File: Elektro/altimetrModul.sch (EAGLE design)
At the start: 16 parts, among them IC1 ATTINY1624-SSU, J1 SM04B-GHS-TB(LF)(SN)-

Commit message: Added Modules
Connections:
- net MISO: now also JP4.3
- net MOSI: no longer JP4.3
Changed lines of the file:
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@@
 <pinref part="JP2" gate="A" pin="6"/>
+</segment>
+<segment>
+<pinref part="JP4" gate="A" pin="3"/>
+<wire x1="-43.18" y1="48.26" x2="-50.8" y2="48.26" width="0.1524" layer="91"/>
+<label x="-50.8" y="48.26" size="1.27" layer="95" rot="R180" xref="yes"/>
 </segment>
 </net>
@@
 </segment>
 <segment>
-<wire x1="-43.18" y1="48.26" x2="-50.8" y2="48.26" width="0.1524" layer="91" grouprefs="FLASH"/>
-<label x="-50.8" y="48.26" size="1.27" layer="95" rot="R180" xref="yes" grouprefs="FLASH"/>
-<pinref part="JP4" gate="A" pin="3"/>
-</segment>
-<segment>

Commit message: Added names
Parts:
- renumbered JP2 to BMP_280, JP4 to FLASH_
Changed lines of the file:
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@@
 <part name="U$8" library="supply2" deviceset="+3.3V" device=""/>
 <part name="GND1" library="PUTRocketLab_supply" deviceset="GND" device=""/>
-<part name="JP2" library="pinhead" library_urn="urn:adsk.eagle:library:325" deviceset="PINHD-1X6" device="" package3d_urn="urn:adsk.eagle:package:22472/2"/>
-<part name="JP4" library="pinhead" library_urn="urn:adsk.eagle:library:325" deviceset="PINHD-1X6" device="" package3d_urn="urn:adsk.eagle:package:22472/2"/>
+<part name="BMP_280" library="pinhead" library_urn="urn:adsk.eagle:library:325" deviceset="PINHD-1X6" device="" package3d_urn="urn:adsk.eagle:package:22472/2"/>
+<part name="FLASH_" library="pinhead" library_urn="urn:adsk.eagle:library:325" deviceset="PINHD-1X6" device="" package3d_urn="urn:adsk.eagle:package:22472/2"/>
 <part name="U$5" library="supply2" deviceset="+3.3V" device=""/>
 <part name="U$7" library="supply2" deviceset="+3.3V" device=""/>
@@
 <attribute name="VALUE" x="-160.02" y="36.83" size="1.778" layer="96"/>
 </instance>
-<instance part="JP2" gate="A" x="60.96" y="96.52" smashed="yes" grouprefs="BMP280">
+<instance part="BMP_280" gate="A" x="60.96" y="96.52" smashed="yes" grouprefs="BMP280">
 <attribute name="NAME" x="54.61" y="107.315" size="1.778" layer="95"/>
 <attribute name="VALUE" x="54.61" y="86.36" size="1.778" layer="96"/>
 </instance>
-<instance part="JP4" gate="A" x="-40.64" y="45.72" smashed="yes" grouprefs="FLASH">
+<instance part="FLASH_" gate="A" x="-40.64" y="45.72" smashed="yes" grouprefs="FLASH">
 <attribute name="NAME" x="-46.99" y="56.515" size="1.778" layer="95"/>
 <attribute name="VALUE" x="-46.99" y="35.56" size="1.778" layer="96"/>
@@
 </segment>
 <segment>
-<pinref part="JP2" gate="A" pin="2"/>
+<pinref part="BMP_280" gate="A" pin="2"/>
 <pinref part="GND5" gate="1" pin="GND"/>
 <wire x1="38.1" y1="101.6" x2="58.42" y2="101.6" width="0.1524" layer="91" grouprefs="BMP280"/>
@@
 <pinref part="GND8" gate="1" pin="GND"/>
 <wire x1="-60.96" y1="43.18" x2="-60.96" y2="45.72" width="0.1524" layer="91" grouprefs="FLASH"/>
-<pinref part="JP4" gate="A" pin="4"/>
+<pinref part="FLASH_" gate="A" pin="4"/>
 <wire x1="-60.96" y1="45.72" x2="-43.18" y2="45.72" width="0.1524" layer="91" grouprefs="FLASH"/>
 </segment>
@@
 </segment>
 <segment>
-<pinref part="JP2" gate="A" pin="1"/>
+<pinref part="BMP_280" gate="A" pin="1"/>
 <wire x1="58.42" y1="104.14" x2="50.8" y2="104.14" width="0.1524" layer="91" grouprefs="BMP280"/>
 <pinref part="U$5" gate="G$1" pin="+3.3V"/>
 </segment>
 <segment>
-<pinref part="JP4" gate="A" pin="1"/>
+<pinref part="FLASH_" gate="A" pin="1"/>
 <wire x1="-43.18" y1="53.34" x2="-50.8" y2="53.34" width="0.1524" layer="91" grouprefs="FLASH"/>
 <pinref part="U$7" gate="G$1" pin="+3.3V"/>
@@
 <wire x1="58.42" y1="99.06" x2="50.8" y2="99.06" width="0.1524" layer="91" grouprefs="BMP280"/>
 <label x="50.8" y="99.06" size="1.27" layer="95" rot="R180" xref="yes" grouprefs="BMP280"/>
-<pinref part="JP2" gate="A" pin="3"/>
+<pinref part="BMP_280" gate="A" pin="3"/>
 </segment>
 <segment>
 <wire x1="-43.18" y1="43.18" x2="-50.8" y2="43.18" width="0.1524" layer="91" grouprefs="FLASH"/>
 <label x="-50.8" y="43.18" size="1.27" layer="95" rot="R180" xref="yes" grouprefs="FLASH"/>
-<pinref part="JP4" gate="A" pin="5"/>
+<pinref part="FLASH_" gate="A" pin="5"/>
 </segment>
 </net>
@@
 <wire x1="58.42" y1="91.44" x2="50.8" y2="91.44" width="0.1524" layer="91" grouprefs="BMP280"/>
 <label x="50.8" y="91.44" size="1.27" layer="95" rot="R180" xref="yes" grouprefs="BMP280"/>
-<pinref part="JP2" gate="A" pin="6"/>
-</segment>
-<segment>
-<pinref part="JP4" gate="A" pin="3"/>
+<pinref part="BMP_280" gate="A" pin="6"/>
+</segment>
+<segment>
+<pinref part="FLASH_" gate="A" pin="3"/>
 <wire x1="-43.18" y1="48.26" x2="-50.8" y2="48.26" width="0.1524" layer="91"/>
 <label x="-50.8" y="48.26" size="1.27" layer="95" rot="R180" xref="yes"/>
@@
 <wire x1="58.42" y1="96.52" x2="50.8" y2="96.52" width="0.1524" layer="91" grouprefs="BMP280"/>
 <label x="50.8" y="96.52" size="1.27" layer="95" rot="R180" xref="yes" grouprefs="BMP280"/>
-<pinref part="JP2" gate="A" pin="4"/>
+<pinref part="BMP_280" gate="A" pin="4"/>
 </segment>
 <segment>
 <wire x1="-43.18" y1="40.64" x2="-50.8" y2="40.64" width="0.1524" layer="91" grouprefs="FLASH"/>
 <label x="-50.8" y="40.64" size="1.27" layer="95" rot="R180" xref="yes" grouprefs="FLASH"/>
-<pinref part="JP4" gate="A" pin="6"/>
+<pinref part="FLASH_" gate="A" pin="6"/>
 </segment>
 </net>
@@
 <wire x1="58.42" y1="93.98" x2="50.8" y2="93.98" width="0.1524" layer="91" grouprefs="BMP280"/>
 <label x="50.8" y="93.98" size="1.27" layer="95" rot="R180" xref="yes" grouprefs="BMP280"/>
-<pinref part="JP2" gate="A" pin="5"/>
+<pinref part="BMP_280" gate="A" pin="5"/>
 </segment>
 </net>
@@
 <wire x1="-43.18" y1="50.8" x2="-50.8" y2="50.8" width="0.1524" layer="91" grouprefs="FLASH"/>
 <label x="-50.8" y="50.8" size="1.27" layer="95" rot="R180" xref="yes" grouprefs="FLASH"/>
-<pinref part="JP4" gate="A" pin="2"/>
-</segment>
-</net>
+<pinref part="FLASH_" gate="A" pin="2"/>
+</segment>
+</net>

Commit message: Gerber generated in .zip
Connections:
- removed net WP: IC1.PA4
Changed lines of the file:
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@@
-</segment>
-</net>
-<net name="WP" class="0">
-<segment>
-<pinref part="IC1" gate="G$1" pin="PA4"/>
-<wire x1="-53.34" y1="101.6" x2="-55.88" y2="101.6" width="0.1524" layer="91" grouprefs="ATTINY"/>
-<label x="-55.88" y="101.6" size="1.778" layer="95" rot="R180" xref="yes" grouprefs="ATTINY"/>
 </segment>
 </net>

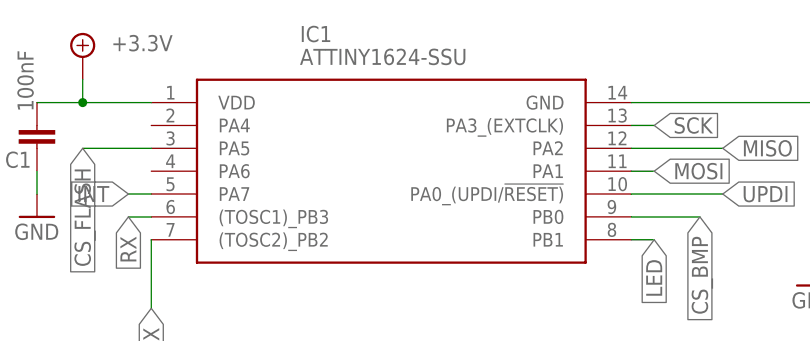
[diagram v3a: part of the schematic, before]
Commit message: ATtiny 1624 changed to ATtiny 3224 (the memory size too small for all of the functionalities of the program
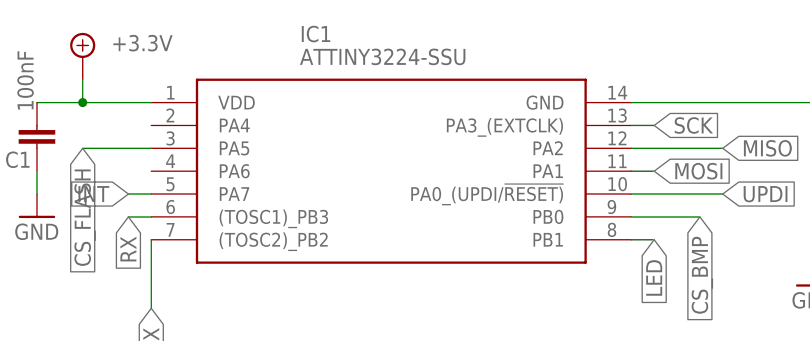
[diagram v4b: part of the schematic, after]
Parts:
- IC1: value ATTINY1624-SSU -> ATTINY3224-SSU; device ATTINY1624-SSU:ATTINY1624-SSU -> ATTINY3224-SSU:ATTINY3224-SSU
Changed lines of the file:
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@@
 <part name="LED1" library="led" library_urn="urn:adsk.eagle:library:259" deviceset="LED" device="CHIP-LED0805" package3d_urn="urn:adsk.eagle:package:15818/2"/>
 <part name="R1" library="rcl" library_urn="urn:adsk.eagle:library:334" deviceset="R-EU_" device="R0805" package3d_urn="urn:adsk.eagle:package:23553/2" value="470R"/>
-<part name="IC1" library="ATTINY1624-SSU" deviceset="ATTINY1624-SSU" device=""/>
+<part name="IC1" library="ATTINY3224-SSU" deviceset="ATTINY3224-SSU" device=""/>
 <part name="GND2" library="PUTRocketLab_supply" deviceset="GND" device=""/>
 <part name="GND3" library="PUTRocketLab_supply" deviceset="GND" device=""/>
